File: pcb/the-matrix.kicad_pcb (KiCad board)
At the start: 4 copper layers, 102 x 102 mm, 81 parts, among them J1 DNP, J2 DNP, J3 Conn_02x20_Odd_Even, J4 Conn_02x20_Odd_Even, J5 Conn_02x20_Odd_Even, J6 Conn_02x20_Odd_Even, Q1 Q_PMOS_GDS, Q10 Q_PMOS_GDS, Q11 Q_PMOS_GDS, Q12 Q_PMOS_GDS, Q13 Q_PMOS_GDS, Q14 Q_PMOS_GDS, Q15 Q_PMOS_GDS, Q16 Q_PMOS_GDS, Q17 Q_PMOS_GDS, Q18 Q_PMOS_GDS, Q19 Q_PMOS_GDS, Q2 Q_PMOS_GDS, Q20 Q_PMOS_GDS, Q21 Q_PMOS_GDS, Q22 Q_PMOS_GDS, Q23 Q_PMOS_GDS, Q24 Q_PMOS_GDS, Q25 Q_PMOS_GDS, Q26 Q_PMOS_GDS, Q27 Q_PMOS_GDS, Q28 Q_PMOS_GDS, Q29 Q_PMOS_GDS, Q3 Q_PMOS_GDS, Q30 Q_PMOS_GDS, Q31 Q_PMOS_GDS, Q32 Q_PMOS_GDS, Q33 Q_PMOS_GDS, Q34 Q_PMOS_GDS, Q35 Q_PMOS_GDS, Q36 Q_PMOS_GDS, Q37 Q_PMOS_GDS, Q38 Q_PMOS_GDS, Q39 Q_PMOS_GDS, Q4 Q_PMOS_GDS, Q40 Q_PMOS_GDS, Q5 Q_PMOS_GDS, Q6 Q_PMOS_GDS, Q7 Q_PMOS_GDS, Q8 Q_PMOS_GDS, Q9 Q_PMOS_GDS, U1 74HC595, U10 TPIC6B595N, U2 74HC595, U3 74HC595, U4 74HC595, U5 74HC595, U6 TPIC6B595N, U7 TPIC6B595N, U8 TPIC6B595N, U9 TPIC6B595N

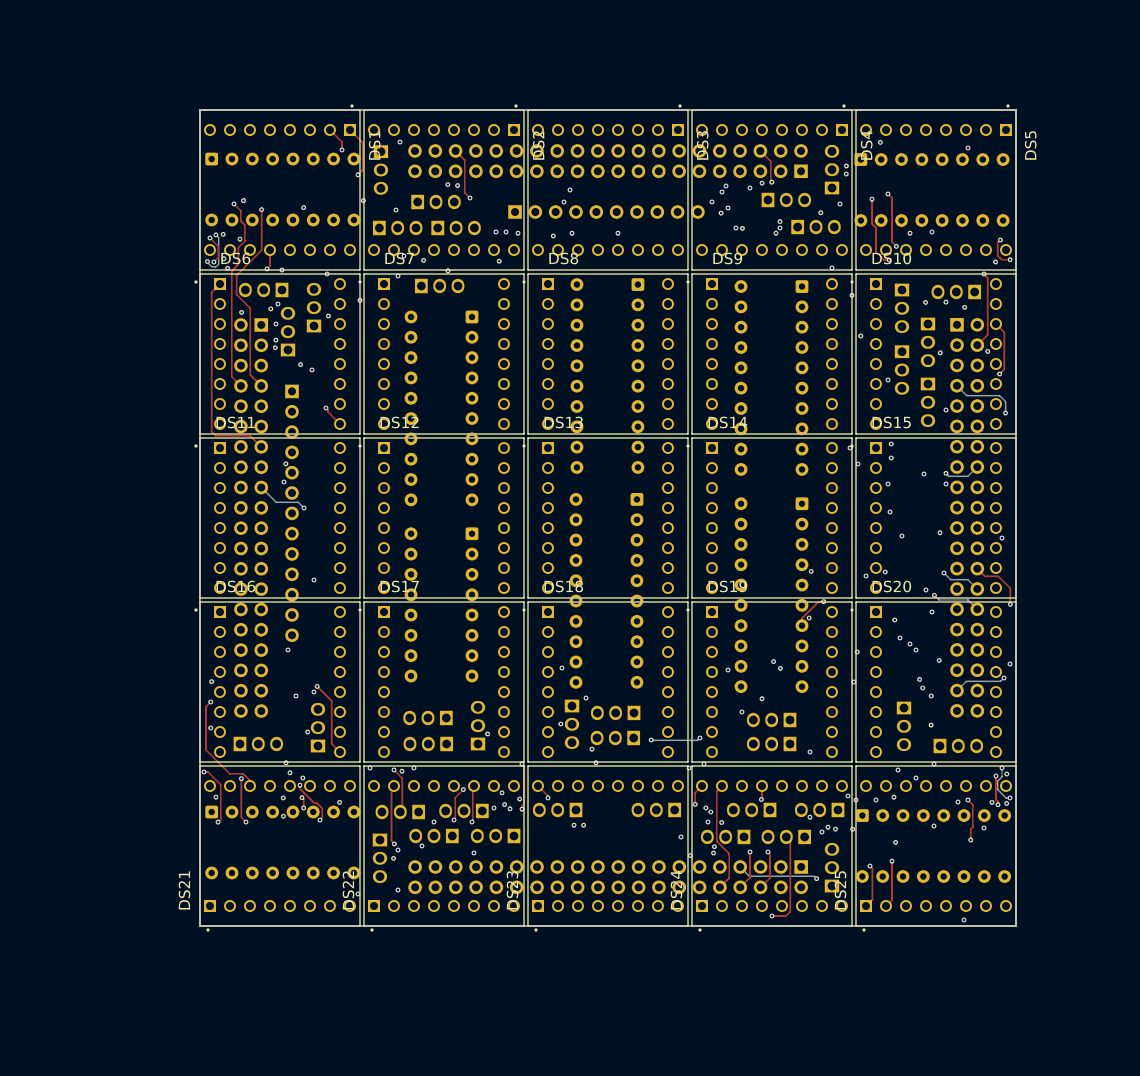
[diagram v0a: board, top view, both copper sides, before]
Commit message: start connecting the shift registers
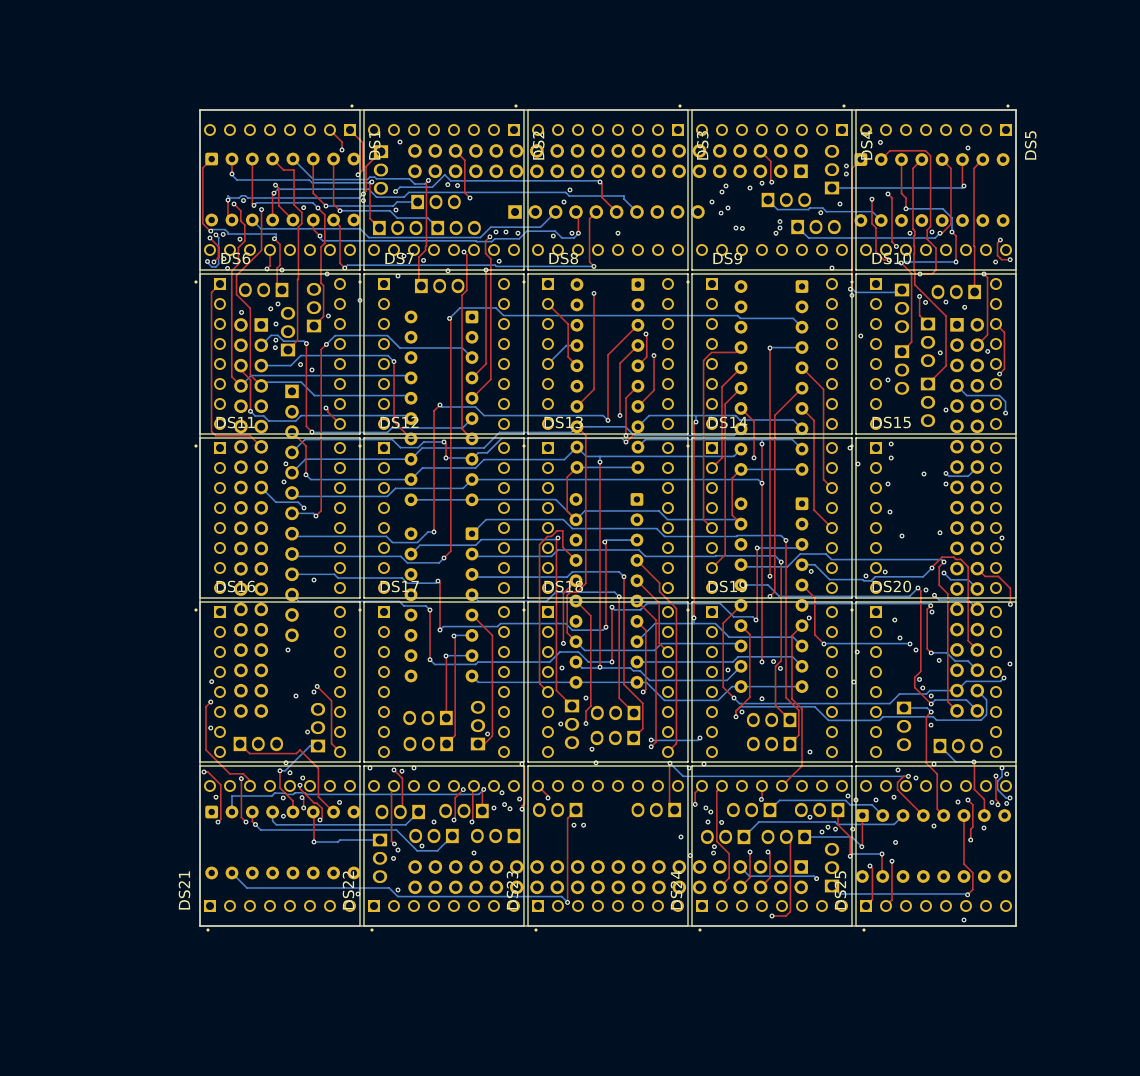
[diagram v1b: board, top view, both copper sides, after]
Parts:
- moved U10 20.6 mm to (181.8, 80.5)
- moved U9 20.6 mm to (161.1, 79.9)
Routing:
- net /ROWEN: track 0.00 -> 131.2 mm, vias 0 -> 3
- net /ROWCLR: track 0.00 -> 119.5 mm, vias 0 -> 5
- net GND: track 0.00 -> 117.2 mm
- net /ROWCLK: track 0.00 -> 112.5 mm, vias 0 -> 3
- net /ROWLATCH: track 0.00 -> 110.1 mm
- net /ROWDAT2: track 0.00 -> 95.7 mm, vias 0 -> 2
- net /ROWDAT4: track 0.00 -> 89.6 mm, vias 0 -> 6
- net /ROWDAT1: track 0.00 -> 70.2 mm, vias 0 -> 3
- net Net-(Q18-G): track 0.00 -> 67.7 mm, vias 0 -> 1
- net /ROWDAT3: track 0.00 -> 61.4 mm, vias 0 -> 4
- net Net-(Q19-G): track 0.00 -> 60.6 mm, vias 0 -> 1
- net Net-(Q9-G): track 0.00 -> 55.5 mm, vias 0 -> 1
- net /COLLATCH: track 0.00 -> 52.6 mm, vias 0 -> 3
- net /COLEN: track 0.00 -> 50.9 mm, vias 0 -> 1
- net /ROWA36: track 166.3 -> 216.0 mm, vias 5 -> 6
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
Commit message: just starting to route power
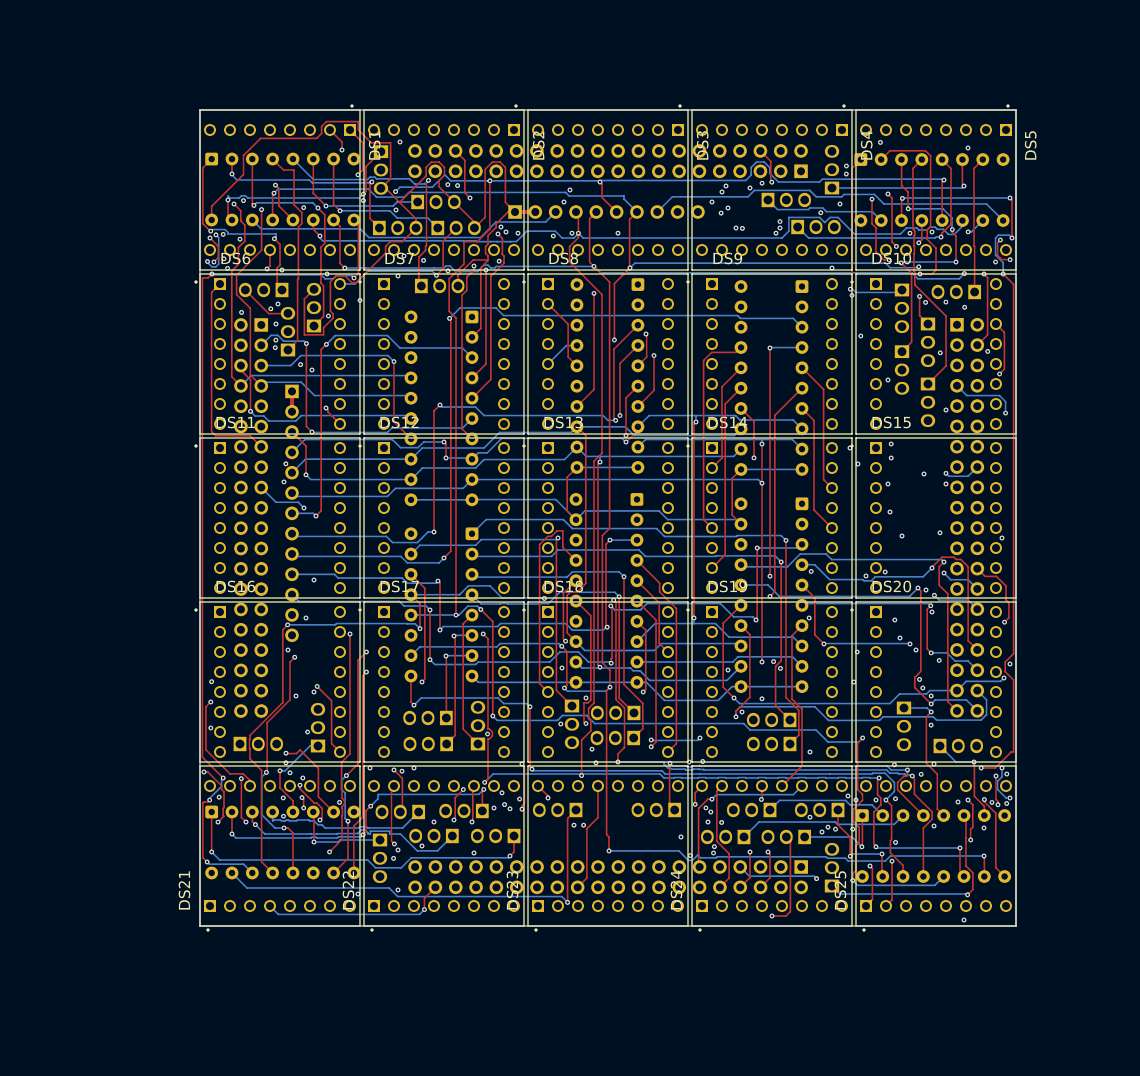
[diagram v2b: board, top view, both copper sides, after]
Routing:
- net /COLCLK: track 39.0 -> 308.5 mm, vias 2 -> 10
- net /COLLATCH: track 52.6 -> 316.2 mm, vias 3 -> 14
- net /COLCLR: track 45.3 -> 295.5 mm, vias 2 -> 12
- net /COLEN: track 50.9 -> 300.0 mm, vias 1 -> 11
- net +5V: track 0.00 -> 147.6 mm
- net Net-(U4-QH'): track 0.00 -> 109.8 mm, vias 0 -> 6
- net Net-(U1-QH'): track 0.00 -> 109.2 mm, vias 0 -> 5
- net Net-(U3-QH'): track 0.00 -> 86.3 mm, vias 0 -> 4
- net Net-(U2-QH'): track 0.00 -> 47.8 mm, vias 0 -> 2
- net Net-(Q10-G): track 0.00 -> 46.4 mm, vias 0 -> 2
- net /COLDATOUT: track 0.00 -> 46.2 mm
- net /COLA2: track 143.5 -> 166.8 mm, vias 3 -> 4
- net /COLA29: track 102.9 -> 124.3 mm, vias 2 -> 3
- net /COLA7: track 131.5 -> 151.6 mm, vias 3 -> 4
- net /COLA16: track 112.6 -> 126.3 mm
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
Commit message: almost there, but when did i delete a display?
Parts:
- removed DS2: TA08-81GWA, snapmagic:DISPLAY_TA08-81GWA
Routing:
- net GND: track 117.2 -> 724.0 mm, vias 0 -> 1
- net +5V: track 147.6 -> 416.1 mm
- net /COLA5: track 125.7 -> 151.1 mm, vias 3 -> 5
- net Net-(Q37-G): track 31.3 -> 29.4 mm
- net /ROWA7: track 198.7 -> 199.7 mm
- net /COLDATOUT: track 46.2 -> 46.8 mm
- net Net-(U4-QH'): track 109.8 -> 110.4 mm
- net Net-(Q36-G): track 37.2 -> 37.8 mm
- net /COLA13: track 147.1 -> 147.0 mm, vias 3 -> 4
- net /ROWA3: vias 6 -> 7
- net /COLA11: vias 4 -> 5
- added copper zone on F.Cu, net +5V
- added copper zone on B.Cu, net GND

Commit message: dw the display is fine
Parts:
- added DS2: TA08-81GWA, snapmagic:DISPLAY_TA08-81GWA, F.Cu at (137.0, 41.2)

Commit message: pcb complete!
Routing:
- net /ROWA3: vias 7 -> 6
- net /COLA13: vias 4 -> 3
- net /COLA11: vias 5 -> 4
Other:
- board text added: "COLUMN CONTROL"
- board text added: "LEFT >"
- board text added: "^ UP"
